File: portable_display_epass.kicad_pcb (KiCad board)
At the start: 4 copper layers, 58 x 110 mm, 115 parts, among them J1 USB4105-GF-A-060, J2 1S LiPo + NTC, J3 DEBUG POGO, J4 TFT-H035B22WVIST8N20_V3-0, J5 MicroSD, Q1 2N7002, Q2 2N7002, Q3 AO3401A, SW1 UP, SW2 DOWN, SW3 OK, SW4 BACK, SW5 POWER, SW6 FEL, U1 AXP2101, U2 V851s, U3 W25N01GVZEIG, U4 LIS2DW12TR, U5 RV-3028-C7, U6 SN74LVC1G123DCTR, U7 TPS61169DCKR, U8 TPS22918DBVR, U9 USBLC6-2SC6, Y1 24MHz 10ppm

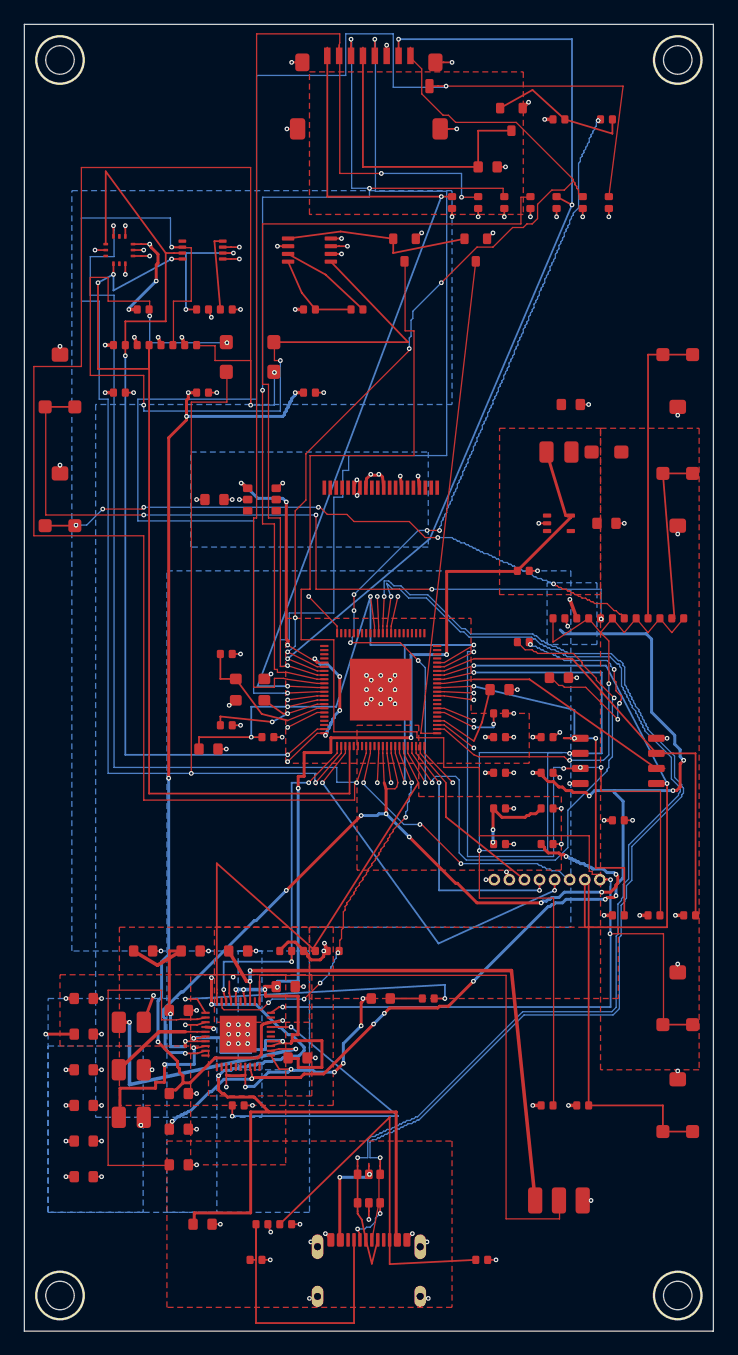
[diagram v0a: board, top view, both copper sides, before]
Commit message: wip(pcb): place KD024 FPC45 + TPS65631 display island
- J4 FPC20→FPC45 at (34,38); U10 + L5/L6 + EL/VCI caps placed
- Local EL Cout copper only; MIPI/control/J4 feeds still ratsnest
- Cleared pocket copper under new island (SD/KEY restore needed)
- DRC: 7 copper / 81 unconnected / 27 parity; fabrication_released false
- See docs/DISPLAY_PCB_STATUS.md
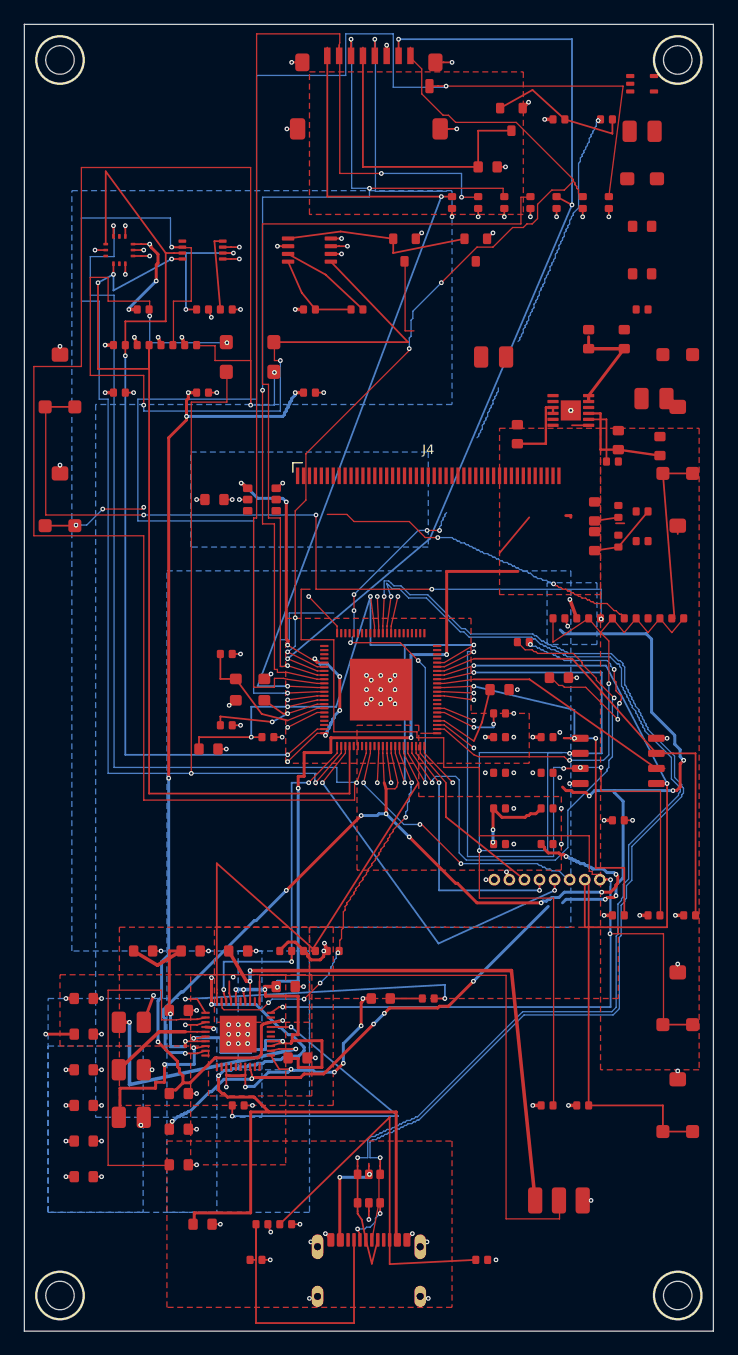
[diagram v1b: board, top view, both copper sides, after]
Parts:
- added C42: 1u, Sameat:0603, F.Cu at (48.0, 41.0)
- added C43: 100n, Sameat:0402, F.Cu at (50.0, 41.0)
- added C44: 1u, Sameat:0603, F.Cu at (48.0, 43.5)
- added C45: 100n, Sameat:0402, F.Cu at (50.0, 43.5)
- added C46: 10u, Sameat:0603, F.Cu at (47.5, 26.5)
- added C47: 10u, Sameat:0603, F.Cu at (50.5, 26.5)
- added C48: 10u, Sameat:0603, F.Cu at (41.5, 34.5)
- added C49: 10u, Sameat:0603, F.Cu at (50.0, 35.0)
- added C50: 10u, Sameat:0603, F.Cu at (53.5, 35.5)
- added C51: 100n, Sameat:0402, F.Cu at (49.5, 36.8)
- added L5: 4.7uH, Sameat:IND_2x2, F.Cu at (39.5, 28.0)
- added L6: 4.7uH, Sameat:IND_2x2, F.Cu at (53.0, 31.5)
- added R29: 0R, Sameat:0402, F.Cu at (52.0, 41.0)
- added R31: 0R, Sameat:0402, F.Cu at (52.0, 43.5)
- added U10: TPS65631DPDR, Sameat:WSON-12, F.Cu at (46.0, 32.5)
- J4: value TFT-H035B22WVIST8N20_V3-0 -> KD024EGOIN152-01; footprint Sameat:FPC20 -> Sameat:FPC45
- moved U7 37.7 mm to (52.0, 5.00)
- moved L4 27.9 mm to (52.0, 9.00)
- moved R19 25.2 mm to (52.0, 17.0)
- moved C28 24.2 mm to (52.0, 24.0)
- moved D4 23.2 mm to (52.0, 13.0)
- moved C27 12.5 mm to (52.0, 21.0)
- moved J4 4.12 mm to (34.0, 38.0)
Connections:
- C27 pad 1: LEDA -> (no net)
- C27 pad 2: GND -> (no net)
- C28 pad 1: VSYS -> (no net)
- C28 pad 2: GND -> (no net)
- D4 pad 1: BL_SW -> (no net)
- D4 pad 2: LEDA -> (no net)
- J4 pad 1: unconnected-(J4-PIN1-Pad1) -> GND
- J4 pad 10: DSI_D1N -> GND
- J4 pad 11: GND -> LCD_1V8
- J4 pad 12: DSI_CKP -> GND
- J4 pad 13: DSI_CKN -> LCD_TE1
- J4 pad 14: GND -> LCD_SWIRE
- J4 pad 15: DSI_D0P -> LCD_TE
- J4 pad 16: DSI_D0N -> LCD_RST
- J4 pad 18: LCD_RST -> (no net)
- J4 pad 19: LEDK -> (no net)
- J4 pad 2: unconnected-(J4-PIN2-Pad2) -> GND
- J4 pad 20: LEDA -> (no net)
- J4 pad 3: unconnected-(J4-PIN3-Pad3) -> ELVSS
- J4 pad 4: unconnected-(J4-PIN4-Pad4) -> ELVSS
- J4 pad 5: unconnected-(J4-PIN5-Pad5) -> GND
- J4 pad 6: LCD_3V3 -> ELVDD
- J4 pad 7: LCD_3V3 -> ELVDD
- J4 pad 9: DSI_D1P -> LCD_3V3
- L4 pad 1: VSYS -> (no net)
- L4 pad 2: BL_SW -> (no net)
- R19 pad 1: LEDK -> (no net)
- R19 pad 2: GND -> (no net)
- U2 pad 3: LCD_PWM -> LCD_TE
- U7 pad 1: BL_SW -> (no net)
- U7 pad 2: GND -> (no net)
- U7 pad 3: LEDK -> (no net)
- U7 pad 4: LCD_PWM -> (no net)
- U7 pad 5: VSYS -> (no net)
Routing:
- net SD_CLK: track 142.2 -> 97.2 mm
- net WAKE_PULSE_N: track 41.4 -> 1.38 mm
- net PWRON_N: track 147.2 -> 116.7 mm
- net KEY_OK: track 25.9 -> 0.00 mm
- net GND: track 76.0 -> 59.6 mm, vias 115 -> 106
- net KEY_DOWN: track 53.3 -> 37.6 mm, vias 6 -> 5
- net SD_PWR_EN: track 74.2 -> 62.3 mm
- net LCD_1V8: track 0.00 -> 9.83 mm
- net ELVSS: track 0.00 -> 9.09 mm
- net ELVDD: track 0.00 -> 6.55 mm
- net 1V8: track 94.0 -> 88.9 mm
- net EL_CT: track 0.00 -> 5.05 mm
- net VSYS: track 124.8 -> 128.8 mm
- net LCD_EN: track 0.00 -> 1.40 mm
- net LCD_3V3: track 2.80 -> 3.42 mm, vias 4 -> 2

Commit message: grok-says-yes
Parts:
- removed C27: 1u/25V, Sameat:0603
- removed C28: 100n, Sameat:0402
- removed D4: SS16, Sameat:D_SOD123
- removed L4: 10uH/1.5A, Sameat:IND_2x2
- removed R19: 2.55R 1%, Sameat:0603
- removed U7: TPS61169DCKR, Sameat:SC70-5
- moved C42 23.0 mm to (25.0, 42.0)
- moved C43 23.0 mm to (27.0, 42.0)
- moved R29 22.4 mm to (30.0, 45.0)
- moved C44 18.1 mm to (30.0, 42.0)
- moved C45 18.1 mm to (32.0, 42.0)
- moved R31 17.1 mm to (35.0, 42.0)
- moved L6 4.30 mm to (50.5, 28.0)
- moved J4 4.12 mm to (30.0, 39.0)
- moved C49 3.50 mm to (50.0, 31.5)
- moved C48 3.04 mm to (42.0, 31.5)
- moved C51 2.51 mm to (48.5, 34.5)
- moved U10 2.50 mm to (46.0, 30.0)
- moved C50 2.12 mm to (52.0, 34.0)
- moved L5 2.00 mm to (41.5, 28.0)
- moved C46 1.80 mm to (46.0, 25.5), turned to 0 degrees
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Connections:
- J4 pad 13: LCD_TE1 -> unconnected-(J4-TE1-Pad13)
- J4 pad 18: (no net) -> unconnected-(J4-PIN18-Pad18)
- J4 pad 19: (no net) -> unconnected-(J4-PIN19-Pad19)
- J4 pad 20: (no net) -> unconnected-(J4-PIN20-Pad20)
- J4 pad 21: (no net) -> unconnected-(J4-PIN21-Pad21)
- J4 pad 22: (no net) -> unconnected-(J4-PIN22-Pad22)
- J4 pad 23: (no net) -> unconnected-(J4-PIN23-Pad23)
- J4 pad 24: (no net) -> unconnected-(J4-PIN24-Pad24)
- J4 pad 25: (no net) -> unconnected-(J4-PIN25-Pad25)
- J4 pad 26: (no net) -> unconnected-(J4-PIN26-Pad26)
- J4 pad 27: (no net) -> unconnected-(J4-PIN27-Pad27)
- J4 pad 28: (no net) -> unconnected-(J4-PIN28-Pad28)
- J4 pad 29: (no net) -> unconnected-(J4-PIN29-Pad29)
- U2 pad 82: DSI_D1N -> unconnected-(U2-PD3_DSI_D1N-Pad82)
- U2 pad 83: DSI_D1P -> unconnected-(U2-PD4_DSI_D1P-Pad83)
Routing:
- net LCD_EN: track 1.40 -> 186.7 mm, vias 0 -> 22
- net KEY_DOWN: track 37.6 -> 97.8 mm, vias 5 -> 10
- net WAKE_PULSE_N: track 1.38 -> 51.2 mm, vias 0 -> 4
- net GND: track 59.6 -> 95.2 mm, vias 106 -> 143
- net SD_D1: track 77.1 -> 104.9 mm, vias 4 -> 5
- net ELVSS: track 9.09 -> 36.5 mm, vias 0 -> 2
- net KEY_OK: track 0.00 -> 25.2 mm
- net PWRON_N: track 116.7 -> 141.8 mm, vias 3 -> 5
- net 1V8: track 88.9 -> 113.0 mm, vias 13 -> 16
- net KEY_UP: track 67.0 -> 90.0 mm, vias 4 -> 10
- net ELVDD: track 6.55 -> 28.8 mm, vias 0 -> 6
- net LCD_RST: track 0.00 -> 19.6 mm, vias 0 -> 2
- net DSI_D0P: track 0.00 -> 19.6 mm, vias 0 -> 2
- net DSI_D0N: track 0.00 -> 19.6 mm, vias 0 -> 2
- net DSI_CKN: track 0.00 -> 18.6 mm
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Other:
- board text added: "KD024 MIPI / EL BIAS ENGINEERING CANDIDATE"
- board text removed: "DISPLAY ISLAND FROZEN (MIPI / FPC / backlight)"

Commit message: wip(pcb): relax display island placement and shorten LCD_EN
Study branch only — not fab-ready.
- Move U8 west / U10+EL east; J4 mild north shift
- LCD_EN ~187mm/22vias → ~39mm/0 vias; display F.Cu under U2 → 0
- MIPI 1-lane re-routed short; collateral DRC from channel clears remains
- See docs/DISPLAY_LAYOUT_RELAX.md
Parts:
- moved C46 15.2 mm to (40.0, 39.5)
- moved C47 15.2 mm to (43.0, 39.5)
- moved C48 15.2 mm to (36.0, 45.5)
- moved C49 15.2 mm to (44.0, 45.5)
- moved L5 15.2 mm to (35.5, 42.0)
- moved L6 15.2 mm to (44.5, 42.0)
- moved U10 15.2 mm to (40.0, 44.0)
- moved C51 14.8 mm to (42.5, 48.0)
- moved C50 14.6 mm to (46.5, 47.5)
- moved C44 13.2 mm to (18.0, 47.5)
- moved C45 13.2 mm to (20.0, 47.5)
- moved R31 12.7 mm to (22.5, 44.0)
- moved C43 10.1 mm to (17.5, 45.5)
- moved C42 9.19 mm to (16.5, 45.5)
- moved C29 8.02 mm to (15.5, 48.0)
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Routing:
- net LCD_EN: track 186.7 -> 38.9 mm, vias 22 -> 0
- net GND: track 95.2 -> 160.4 mm, vias 143 -> 158
- net LCD_1V8: track 12.8 -> 26.6 mm, vias 0 -> 2
- net PWRON_N: track 141.8 -> 128.5 mm
- net LCD_3V3: track 20.9 -> 31.3 mm, vias 5 -> 2
- net VSYS: track 146.8 -> 155.9 mm, vias 11 -> 13
- net 1V8: track 113.0 -> 122.1 mm, vias 16 -> 14
- net LCD_TE: track 15.9 -> 23.3 mm
- net LCD_RST: track 19.6 -> 26.3 mm
- net DSI_CKN: track 18.6 -> 24.7 mm
- net DSI_D0N: track 19.6 -> 25.3 mm, vias 2 -> 0
- net KEY_DOWN: track 97.8 -> 92.3 mm
- net SD_D0: track 92.2 -> 87.6 mm
- net SOC_LDO_1V8: track 59.8 -> 55.5 mm, vias 5 -> 4
- net LCD_SWIRE: track 12.3 -> 15.4 mm
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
